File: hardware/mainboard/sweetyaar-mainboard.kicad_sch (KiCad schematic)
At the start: 102 parts, among them Q1 MMBT3904

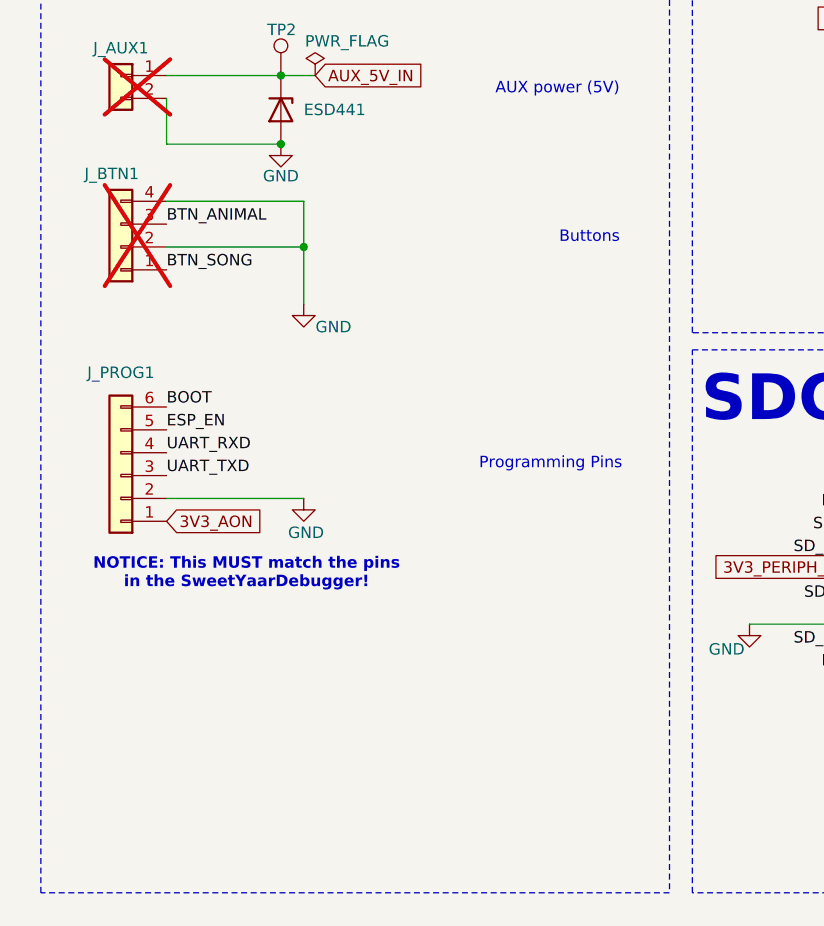
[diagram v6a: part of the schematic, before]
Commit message: adding diodes protection for the ~long cables from the buttons, also adding series resistors
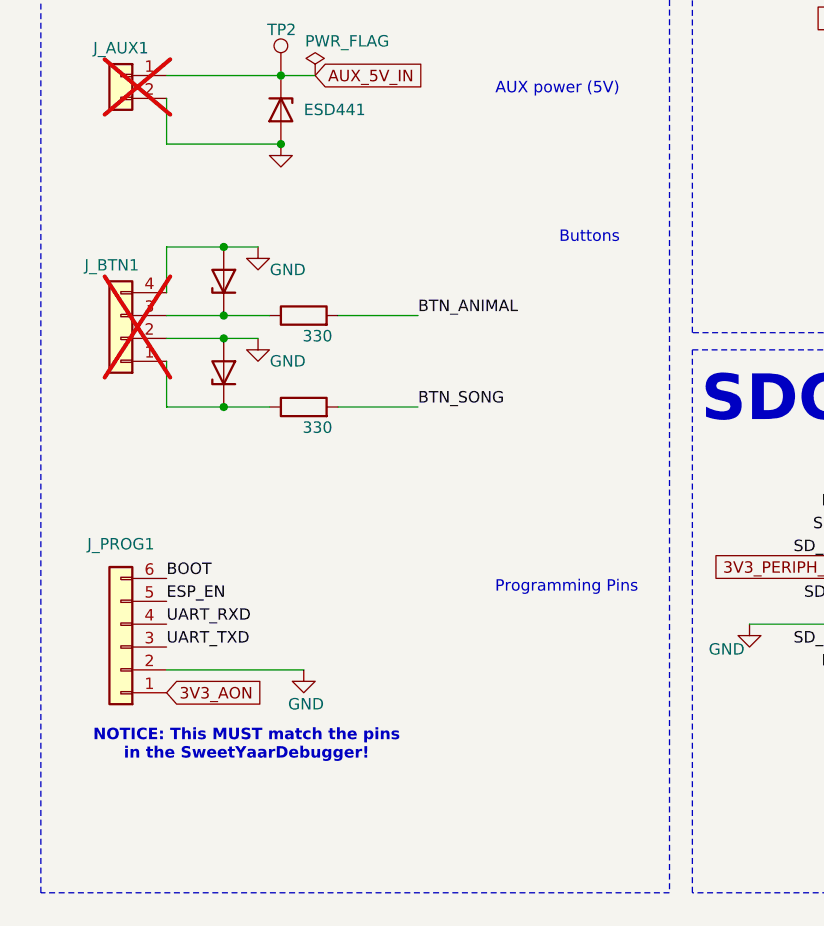
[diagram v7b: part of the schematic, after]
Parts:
- added D3, D5: ESD441, SweetYaar:Texas_DPY0002A_0.6x1mm_P0.65mm, symbol Device:D_Zener
- added R_BTN_ANIMAL1, R_BTN_SONG1: 330, Resistor_SMD:R_0603_1608Metric, symbol Device:R
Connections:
- net BTN_ANIMAL: now also R_BTN_ANIMAL1.2; no longer J_BTN1.3 (Pin_3)
- net BTN_SONG: now also R_BTN_SONG1.2; no longer J_BTN1.1 (Pin_1)
- net GND: now also D3.2 (A), D5.2 (A)
- new net: D3.1 (K), J_BTN1.1 (Pin_1), R_BTN_SONG1.1
- new net: D5.1 (K), J_BTN1.3 (Pin_3), R_BTN_ANIMAL1.1
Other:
- moved on the sheet: J_BTN1, J_PROG1

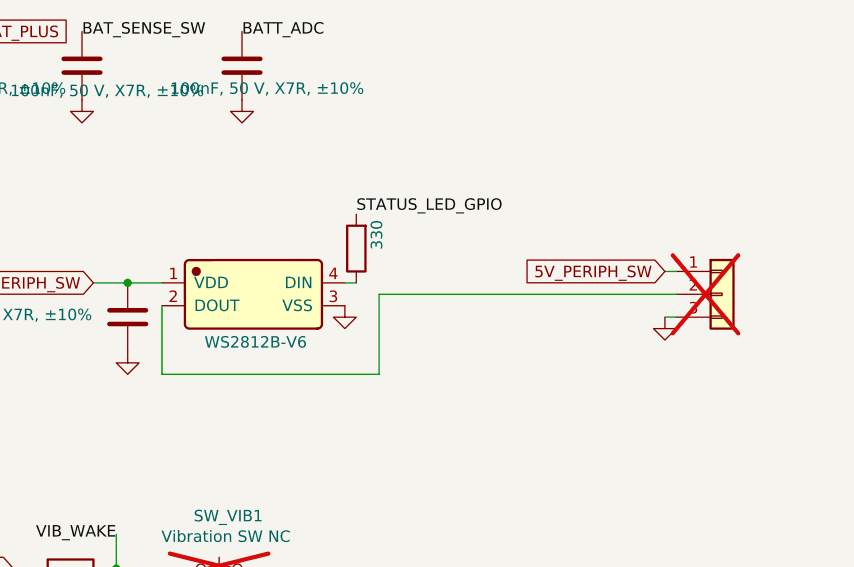
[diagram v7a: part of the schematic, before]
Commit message: Adding a pull-down on LED DIN pin
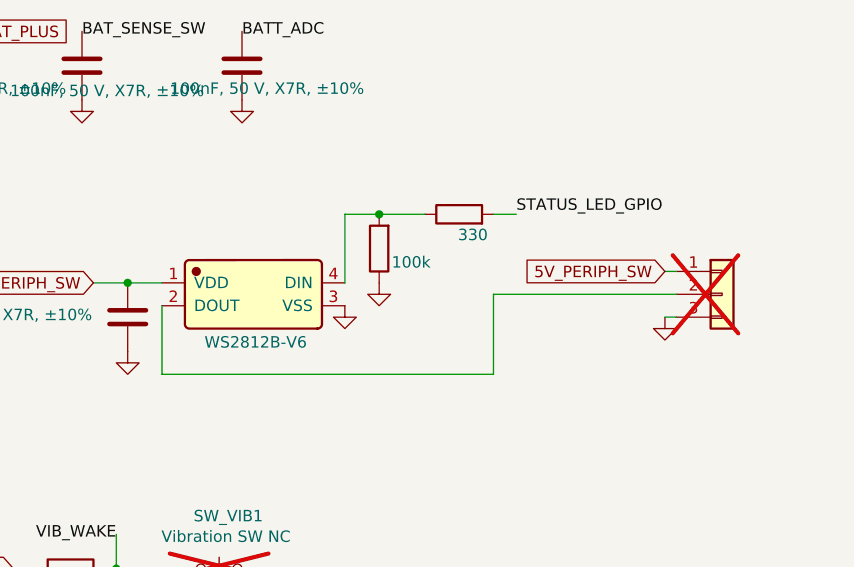
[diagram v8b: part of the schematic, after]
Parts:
- added R_LED_DIN2: 100k, Resistor_SMD:R_0603_1608Metric, symbol Device:R
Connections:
- net GND: now also R_LED_DIN2.1
- net at D_LED1.4 (DIN), R_LED_DIN1.1: now also R_LED_DIN2.2
